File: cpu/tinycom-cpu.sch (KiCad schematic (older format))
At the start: 15 parts, among them P1 CONN_02X08, P2 CONN_02X08, U1 OLIMEX_IC_A13, U2 H5TQ2G83BFR/FBGA82, Y1 Crystal

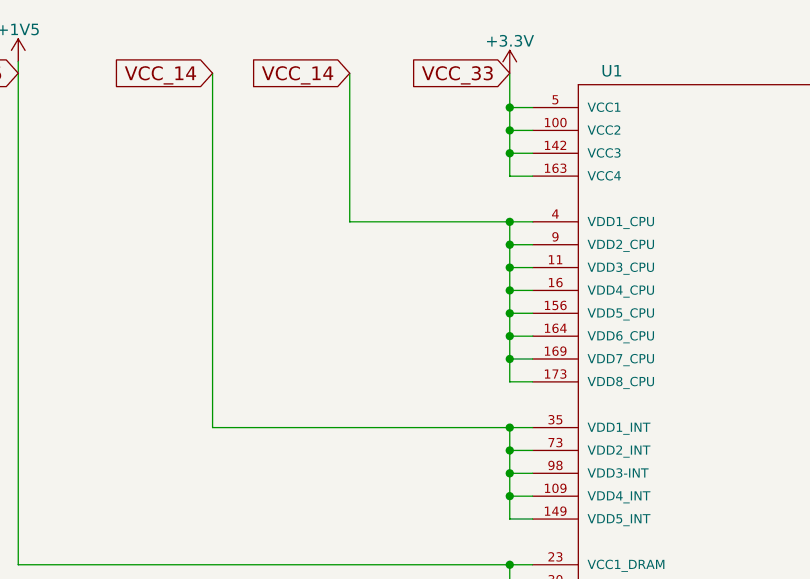
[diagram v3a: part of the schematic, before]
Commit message: add more capacitors
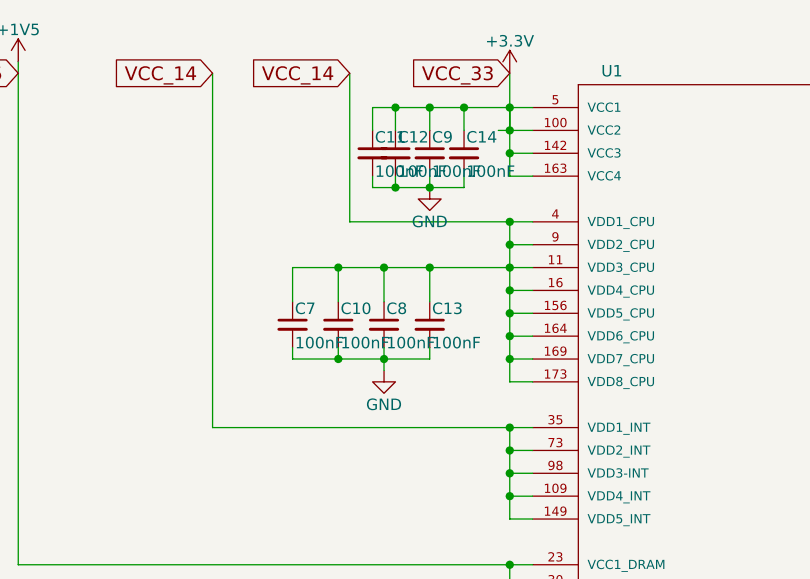
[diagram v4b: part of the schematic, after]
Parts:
- added C10, C11, C12, C13, C14, C7, C8, C9: 100nF, Capacitors_SMD:C_0603, symbol C_Small
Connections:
- net +3V3: now also C11.1, C12.1, C14.1, C9.1
- net GND: now also C10.2, C11.2, C12.2, C13.2, C14.2, C7.2, C8.2, C9.2
- net VCC_14: now also C10.1, C13.1, C7.1, C8.1
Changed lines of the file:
@@
 VCC_33
 $Comp
-L GND #PWR4
+L GND #PWR5
 U 1 1 5624C2D0
 P 1150 2350
-F 0 "#PWR4" H 1150 2100 50  0001 C CNN
+F 0 "#PWR5" H 1150 2100 50  0001 C CNN
 F 1 "GND" H 1150 2200 50  0000 C CNN
 F 2 "" H 1150 2350 60  0000 C CNN
@@
 VCC_14
 $Comp
-L +3.3V #PWR5
+L +3.3V #PWR7
 U 1 1 5624CB40
 P 1550 -1650
-F 0 "#PWR5" H 1550 -1800 50  0001 C CNN
+F 0 "#PWR7" H 1550 -1800 50  0001 C CNN
 F 1 "+3.3V" H 1550 -1510 50  0000 C CNN
 F 2 "" H 1550 -1650 60  0000 C CNN
@@
 DDR3_BA2
 $Comp
-L +1V5 #PWR14
+L +1V5 #PWR16
 U 1 1 5625F72C
 P 9350 -250
-F 0 "#PWR14" H 9350 -400 50  0001 C CNN
+F 0 "#PWR16" H 9350 -400 50  0001 C CNN
 F 1 "+1V5" H 9350 -110 50  0000 C CNN
 F 2 "" H 9350 -250 60  0000 C CNN
@@
 $EndComp
 $Comp
-L GND #PWR15
+L GND #PWR17
 U 1 1 5625F96A
 P 9500 3350
-F 0 "#PWR15" H 9500 3100 50  0001 C CNN
+F 0 "#PWR17" H 9500 3100 50  0001 C CNN
 F 1 "GND" H 9500 3200 50  0000 C CNN
 F 2 "" H 9500 3350 60  0000 C CNN
@@
 DDR3_RST
 $Comp
-L GND #PWR9
+L GND #PWR11
 U 1 1 5625FBB8
 P 5950 2100
-F 0 "#PWR9" H 5950 1850 50  0001 C CNN
+F 0 "#PWR11" H 5950 1850 50  0001 C CNN
 F 1 "GND" H 5950 1950 50  0000 C CNN
 F 2 "" H 5950 2100 60  0000 C CNN
@@
 $EndComp
 $Comp
-L +1V5 #PWR10
+L +1V5 #PWR12
 U 1 1 5625FE07
 P 6150 3250
-F 0 "#PWR10" H 6150 3100 50  0001 C CNN
+F 0 "#PWR12" H 6150 3100 50  0001 C CNN
 F 1 "+1V5" H 6150 3390 50  0000 C CNN
 F 2 "" H 6150 3250 60  0000 C CNN
@@
 $EndComp
 $Comp
-L GND #PWR11
+L GND #PWR13
 U 1 1 5625FF1B
 P 6150 4000
-F 0 "#PWR11" H 6150 3750 50  0001 C CNN
+F 0 "#PWR13" H 6150 3750 50  0001 C CNN
 F 1 "GND" H 6150 3850 50  0000 C CNN
 F 2 "" H 6150 4000 60  0000 C CNN
@@
 $EndComp
 $Comp
-L GND #PWR12
+L GND #PWR14
 U 1 1 56260662
 P 6400 4250
-F 0 "#PWR12" H 6400 4000 50  0001 C CNN
+F 0 "#PWR14" H 6400 4000 50  0001 C CNN
 F 1 "GND" H 6400 4100 50  0000 C CNN
 F 2 "" H 6400 4250 60  0000 C CNN
@@
 NoConn ~ 9250 3500
 $Comp
-L GND #PWR13
+L GND #PWR15
 U 1 1 56261679
 P 6600 4050
-F 0 "#PWR13" H 6600 3800 50  0001 C CNN
+F 0 "#PWR15" H 6600 3800 50  0001 C CNN
 F 1 "GND" H 6600 3900 50  0000 C CNN
 F 2 "" H 6600 4050 60  0000 C CNN
@@
 NoConn ~ 1650 4100
 $Comp
-L GND #PWR6
+L GND #PWR8
 U 1 1 56262629
 P 1550 2500
-F 0 "#PWR6" H 1550 2250 50  0001 C CNN
+F 0 "#PWR8" H 1550 2250 50  0001 C CNN
 F 1 "GND" H 1550 2350 50  0000 C CNN
 F 2 "" H 1550 2500 60  0000 C CNN
@@
 $EndComp
 $Comp
-L GND #PWR8
+L GND #PWR10
 U 1 1 56262930
 P 5550 3750
-F 0 "#PWR8" H 5550 3500 50  0001 C CNN
+F 0 "#PWR10" H 5550 3500 50  0001 C CNN
 F 1 "GND" H 5550 3600 50  0000 C CNN
 F 2 "" H 5550 3750 60  0000 C CNN
@@
 $EndComp
 $Comp
-L GND #PWR7
+L GND #PWR9
 U 1 1 56262D84
 P 5250 4100
-F 0 "#PWR7" H 5250 3850 50  0001 C CNN
+F 0 "#PWR9" H 5250 3850 50  0001 C CNN
 F 1 "GND" H 5250 3950 50  0000 C CNN
 F 2 "" H 5250 4100 60  0000 C CNN
@@
 $EndComp
 $Comp
-L +1V5 #PWR16
+L +1V5 #PWR18
 U 1 1 562642D9
 P 10200 -350
-F 0 "#PWR16" H 10200 -500 50  0001 C CNN
+F 0 "#PWR18" H 10200 -500 50  0001 C CNN
 F 1 "+1V5" H 10200 -210 50  0000 C CNN
 F 2 "" H 10200 -350 60  0000 C CNN
@@
 $EndComp
 $Comp
-L GND #PWR17
+L GND #PWR19
 U 1 1 562643A7
 P 10250 50
-F 0 "#PWR17" H 10250 -200 50  0001 C CNN
+F 0 "#PWR19" H 10250 -200 50  0001 C CNN
 F 1 "GND" H 10250 -100 50  0000 C CNN
 F 2 "" H 10250 50  60  0000 C CNN
@@
 $EndComp
 Wire Wire Line
-	1650 -1500 1550 -1500
+	950  -1500 1650 -1500
 Wire Wire Line
 	1550 -1650 1550 -1200
@@
 Connection ~ 1550 -1300
 Wire Wire Line
-	1650 -1400 1550 -1400
+	1500 -1400 1650 -1400
 Connection ~ 1550 -1400
 Wire Wire Line
@@
 Connection ~ 1550 -700
 Wire Wire Line
-	1650 -800 1550 -800
+	600  -800 1650 -800
 Connection ~ 1550 -800
 Wire Wire Line
@@
 	10250 50   10250 0
 Connection ~ 10250 0
+$Comp
+L C_Small C9
+U 1 1 56265419
+P 1200 -1300
+F 0 "C9" H 1210 -1230 50  0000 L CNN
+F 1 "100nF" H 1210 -1380 50  0000 L CNN
+F 2 "Capacitors_SMD:C_0603" H 1200 -1300 60  0001 C CNN
+F 3 "" H 1200 -1300 60  0000 C CNN
+	1    1200 -1300
+	1    0    0    -1
+$EndComp
+$Comp
+L C_Small C8
+U 1 1 562658F3
+P 1000 -550
+F 0 "C8" H 1010 -480 50  0000 L CNN
+F 1 "100nF" H 1010 -630 50  0000 L CNN
+F 2 "Capacitors_SMD:C_0603" H 1000 -550 60  0001 C CNN
+F 3 "" H 1000 -550 60  0000 C CNN
+	1    1000 -550
+	1    0    0    -1
+$EndComp
+$Comp
+L GND #PWR4
+U 1 1 56265943
+P 1000 -350
+F 0 "#PWR4" H 1000 -600 50  0001 C CNN
+F 1 "GND" H 1000 -500 50  0000 C CNN
+F 2 "" H 1000 -350 60  0000 C CNN
+F 3 "" H 1000 -350 60  0000 C CNN
+	1    1000 -350
+	1    0    0    -1
+$EndComp
+$Comp
+L GND #PWR6
+U 1 1 56265988
+P 1200 -1150
+F 0 "#PWR6" H 1200 -1400 50  0001 C CNN
+F 1 "GND" H 1200 -1300 50  0000 C CNN
+F 2 "" H 1200 -1150 60  0000 C CNN
+F 3 "" H 1200 -1150 60  0000 C CNN
+	1    1200 -1150
+	1    0    0    -1
+$EndComp
+Wire Wire Line
+	1200 -1200 1200 -1150
+Wire Wire Line
+	1000 -450 1000 -350
+Wire Wire Line
+	1550 -1500 1550 -1400
+Wire Wire Line
+	1200 -1400 1200 -1500
+Wire Wire Line
+	1000 -650 1000 -800
+$Comp
+L C_Small C14
+U 1 1 56266A58
+P 1350 -1300
+F 0 "C14" H 1360 -1230 50  0000 L CNN
+F 1 "100nF" H 1360 -1380 50  0000 L CNN
+F 2 "Capacitors_SMD:C_0603" H 1350 -1300 60  0001 C CNN
+F 3 "" H 1350 -1300 60  0000 C CNN
+	1    1350 -1300
+	1    0    0    -1
+$EndComp
+$Comp
+L C_Small C12
+U 1 1 56266AAE
+P 1050 -1300
+F 0 "C12" H 1060 -1230 50  0000 L CNN
+F 1 "100nF" H 1060 -1380 50  0000 L CNN
+F 2 "Capacitors_SMD:C_0603" H 1050 -1300 60  0001 C CNN
+F 3 "" H 1050 -1300 60  0000 C CNN
+	1    1050 -1300
+	1    0    0    -1
+$EndComp
+Wire Wire Line
+	1050 -1500 1050 -1400
+Connection ~ 1200 -1500
+Wire Wire Line
+	1350 -1400 1350 -1500
+Connection ~ 1350 -1500
+Wire Wire Line
+	1050 -1200 1050 -1150
+Wire Wire Line
+	950  -1150 1350 -1150
+Wire Wire Line
+	1350 -1150 1350 -1200
+Connection ~ 1200 -1150
+$Comp
+L C_Small C11
+U 1 1 56267024
+P 950 -1300
+F 0 "C11" H 960 -1230 50  0000 L CNN
+F 1 "100nF" H 960 -1380 50  0000 L CNN
+F 2 "Capacitors_SMD:C_0603" H 950 -1300 60  0001 C CNN
+F 3 "" H 950 -1300 60  0000 C CNN
+	1    950  -1300
+	1    0    0    -1
+$EndComp
+Wire Wire Line
+	950  -1500 950  -1400
+Connection ~ 1050 -1500
+Wire Wire Line
+	950  -1200 950  -1150
+Connection ~ 1050 -1150
+$Comp
+L C_Small C10
+U 1 1 56267401
+P 800 -550
+F 0 "C10" H 810 -480 50  0000 L CNN
+F 1 "100nF" H 810 -630 50  0000 L CNN
+F 2 "Capacitors_SMD:C_0603" H 800 -550 60  0001 C CNN
+F 3 "" H 800 -550 60  0000 C CNN
+	1    800  -550
+	1    0    0    -1
+$EndComp
+$Comp
+L C_Small C13
+U 1 1 56267464
+P 1200 -550
+F 0 "C13" H 1210 -480 50  0000 L CNN
+F 1 "100nF" H 1210 -630 50  0000 L CNN
+F 2 "Capacitors_SMD:C_0603" H 1200 -550 60  0001 C CNN
+F 3 "" H 1200 -550 60  0000 C CNN
+	1    1200 -550
+	1    0    0    -1
+$EndComp
+$Comp
+L C_Small C7
+U 1 1 562674C6
+P 600 -550
+F 0 "C7" H 610 -480 50  0000 L CNN
+F 1 "100nF" H 610 -630 50  0000 L CNN
+F 2 "Capacitors_SMD:C_0603" H 600 -550 60  0001 C CNN
+F 3 "" H 600 -550 60  0000 C CNN
+	1    600  -550
+	1    0    0    -1
+$EndComp
+Wire Wire Line
+	600  -800 600  -650
+Connection ~ 1000 -800
+Wire Wire Line
+	800  -650 800  -800
+Connection ~ 800  -800
+Wire Wire Line
+	1200 -650 1200 -800
+Connection ~ 1200 -800
+Wire Wire Line
+	600  -450 600  -400
+Wire Wire Line
+	600  -400 1200 -400
+Connection ~ 1000 -400
+Wire Wire Line
+	1200 -400 1200 -450
+Wire Wire Line
+	800  -400 800  -450
+Connection ~ 800  -400
 $EndSCHEMATC

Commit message: change to 0805 components
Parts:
- C1, C10, C11, C12, C13, C14, C2, C3, C4, C5, C6, C7, C8, C9: footprint Capacitors_SMD:C_0603 -> Capacitors_SMD:C_0805
- R1, R2, R3, R4: footprint Resistors_SMD:R_0603 -> Resistors_SMD:R_0805
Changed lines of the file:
@@
 VCC_33
 $Comp
-L GND #PWR5
+L GND #PWR01
 U 1 1 5624C2D0
 P 1150 2350
-F 0 "#PWR5" H 1150 2100 50  0001 C CNN
+F 0 "#PWR01" H 1150 2100 50  0001 C CNN
 F 1 "GND" H 1150 2200 50  0000 C CNN
 F 2 "" H 1150 2350 60  0000 C CNN
@@
 $EndComp
 $Comp
-L GND #PWR2
+L GND #PWR02
 U 1 1 5624C74D
 P 550 1900
-F 0 "#PWR2" H 550 1650 50  0001 C CNN
+F 0 "#PWR02" H 550 1650 50  0001 C CNN
 F 1 "GND" H 550 1750 50  0000 C CNN
 F 2 "" H 550 1900 60  0000 C CNN
@@
 $EndComp
 $Comp
-L GND #PWR3
+L GND #PWR03
 U 1 1 5624C778
 P 550 2200
-F 0 "#PWR3" H 550 1950 50  0001 C CNN
+F 0 "#PWR03" H 550 1950 50  0001 C CNN
 F 1 "GND" H 550 2050 50  0000 C CNN
 F 2 "" H 550 2200 60  0000 C CNN
@@
 F 0 "C1" H 810 1920 50  0000 L CNN
 F 1 "33pF" H 810 1770 50  0000 L CNN
-F 2 "Capacitors_SMD:C_0603" H 800 1850 60  0001 C CNN
+F 2 "Capacitors_SMD:C_0805" H 800 1850 60  0001 C CNN
 F 3 "" H 800 1850 60  0000 C CNN
 	1    800  1850
@@
 F 0 "C2" H 810 2220 50  0000 L CNN
 F 1 "33pF" H 810 2070 50  0000 L CNN
-F 2 "Capacitors_SMD:C_0603" H 800 2150 60  0001 C CNN
+F 2 "Capacitors_SMD:C_0805" H 800 2150 60  0001 C CNN
 F 3 "" H 800 2150 60  0000 C CNN
 	1    800  2150
@@
 VCC_14
 $Comp
-L +3.3V #PWR7
+L +3.3V #PWR04
 U 1 1 5624CB40
 P 1550 -1650
-F 0 "#PWR7" H 1550 -1800 50  0001 C CNN
+F 0 "#PWR04" H 1550 -1800 50  0001 C CNN
 F 1 "+3.3V" H 1550 -1510 50  0000 C CNN
 F 2 "" H 1550 -1650 60  0000 C CNN
@@
 $EndComp
 $Comp
-L +1V5 #PWR1
+L +1V5 #PWR05
 U 1 1 5624CB62
 P -600 -1700
-F 0 "#PWR1" H -600 -1850 50  0001 C CNN
+F 0 "#PWR05" H -600 -1850 50  0001 C CNN
 F 1 "+1V5" H -600 -1560 50  0000 C CNN
 F 2 "" H -600 -1700 60  0000 C CNN
@@
 DDR3_BA2
 $Comp
-L +1V5 #PWR16
+L +1V5 #PWR06
 U 1 1 5625F72C
 P 9350 -250
-F 0 "#PWR16" H 9350 -400 50  0001 C CNN
+F 0 "#PWR06" H 9350 -400 50  0001 C CNN
 F 1 "+1V5" H 9350 -110 50  0000 C CNN
 F 2 "" H 9350 -250 60  0000 C CNN
@@
 $EndComp
 $Comp
-L GND #PWR17
+L GND #PWR07
 U 1 1 5625F96A
 P 9500 3350
-F 0 "#PWR17" H 9500 3100 50  0001 C CNN
+F 0 "#PWR07" H 9500 3100 50  0001 C CNN
 F 1 "GND" H 9500 3200 50  0000 C CNN
 F 2 "" H 9500 3350 60  0000 C CNN
@@
 DDR3_RST
 $Comp
-L GND #PWR11
+L GND #PWR08
 U 1 1 5625FBB8
 P 5950 2100
-F 0 "#PWR11" H 5950 1850 50  0001 C CNN
+F 0 "#PWR08" H 5950 1850 50  0001 C CNN
 F 1 "GND" H 5950 1950 50  0000 C CNN
 F 2 "" H 5950 2100 60  0000 C CNN
@@
 $EndComp
 $Comp
-L +1V5 #PWR12
+L +1V5 #PWR09
 U 1 1 5625FE07
 P 6150 3250
-F 0 "#PWR12" H 6150 3100 50  0001 C CNN
+F 0 "#PWR09" H 6150 3100 50  0001 C CNN
 F 1 "+1V5" H 6150 3390 50  0000 C CNN
 F 2 "" H 6150 3250 60  0000 C CNN
@@
 F 0 "R1" V 6230 3450 50  0000 C CNN
 F 1 "1K" V 6150 3450 50  0000 C CNN
-F 2 "Resistors_SMD:R_0603" V 6080 3450 30  0001 C CNN
+F 2 "Resistors_SMD:R_0805" V 6080 3450 30  0001 C CNN
 F 3 "" H 6150 3450 30  0000 C CNN
 	1    6150 3450
@@
 F 0 "R2" V 6230 3800 50  0000 C CNN
 F 1 "1K" V 6150 3800 50  0000 C CNN
-F 2 "Resistors_SMD:R_0603" V 6080 3800 30  0001 C CNN
+F 2 "Resistors_SMD:R_0805" V 6080 3800 30  0001 C CNN
 F 3 "" H 6150 3800 30  0000 C CNN
 	1    6150 3800
@@
 $EndComp
 $Comp
-L GND #PWR13
+L GND #PWR010
 U 1 1 5625FF1B
 P 6150 4000
-F 0 "#PWR13" H 6150 3750 50  0001 C CNN
+F 0 "#PWR010" H 6150 3750 50  0001 C CNN
 F 1 "GND" H 6150 3850 50  0000 C CNN
 F 2 "" H 6150 4000 60  0000 C CNN
@@
 F 0 "R3" V 6480 4050 50  0000 C CNN
 F 1 "240R" V 6400 4050 50  0000 C CNN
-F 2 "Resistors_SMD:R_0603" V 6330 4050 30  0001 C CNN
+F 2 "Resistors_SMD:R_0805" V 6330 4050 30  0001 C CNN
 F 3 "" H 6400 4050 30  0000 C CNN
 	1    6400 4050
@@
 $EndComp
 $Comp
-L GND #PWR14
+L GND #PWR011
 U 1 1 56260662
 P 6400 4250
-F 0 "#PWR14" H 6400 4000 50  0001 C CNN
+F 0 "#PWR011" H 6400 4000 50  0001 C CNN
 F 1 "GND" H 6400 4100 50  0000 C CNN
 F 2 "" H 6400 4250 60  0000 C CNN
@@
 NoConn ~ 9250 3500
 $Comp
-L GND #PWR15
+L GND #PWR012
 U 1 1 56261679
 P 6600 4050
-F 0 "#PWR15" H 6600 3800 50  0001 C CNN
+F 0 "#PWR012" H 6600 3800 50  0001 C CNN
 F 1 "GND" H 6600 3900 50  0000 C CNN
 F 2 "" H 6600 4050 60  0000 C CNN
@@
 NoConn ~ 1650 4100
 $Comp
-L GND #PWR8
+L GND #PWR013
 U 1 1 56262629
 P 1550 2500
-F 0 "#PWR8" H 1550 2250 50  0001 C CNN
+F 0 "#PWR013" H 1550 2250 50  0001 C CNN
 F 1 "GND" H 1550 2350 50  0000 C CNN
 F 2 "" H 1550 2500 60  0000 C CNN
@@
 $EndComp
 $Comp
-L GND #PWR10
+L GND #PWR014
 U 1 1 56262930
 P 5550 3750
-F 0 "#PWR10" H 5550 3500 50  0001 C CNN
+F 0 "#PWR014" H 5550 3500 50  0001 C CNN
 F 1 "GND" H 5550 3600 50  0000 C CNN
 F 2 "" H 5550 3750 60  0000 C CNN
@@
 F 0 "R4" V 5330 3900 50  0000 C CNN
 F 1 "240R" V 5250 3900 50  0000 C CNN
-F 2 "Resistors_SMD:R_0603" V 5180 3900 30  0001 C CNN
+F 2 "Resistors_SMD:R_0805" V 5180 3900 30  0001 C CNN
 F 3 "" H 5250 3900 30  0000 C CNN
 	1    5250 3900
@@
 $EndComp
 $Comp
-L GND #PWR9
+L GND #PWR015
 U 1 1 56262D84
 P 5250 4100
-F 0 "#PWR9" H 5250 3850 50  0001 C CNN
+F 0 "#PWR015" H 5250 3850 50  0001 C CNN
 F 1 "GND" H 5250 3950 50  0000 C CNN
 F 2 "" H 5250 4100 60  0000 C CNN
@@
 F 0 "C3" H 9910 -80 50  0000 L CNN
 F 1 "100nF" H 9910 -230 50  0000 L CNN
-F 2 "Capacitors_SMD:C_0603" H 9900 -150 60  0001 C CNN
+F 2 "Capacitors_SMD:C_0805" H 9900 -150 60  0001 C CNN
 F 3 "" H 9900 -150 60  0000 C CNN
 	1    9900 -150
@@
 F 0 "C4" H 10110 -80 50  0000 L CNN
 F 1 "100nF" H 10110 -230 50  0000 L CNN
-F 2 "Capacitors_SMD:C_0603" H 10100 -150 60  0001 C CNN
+F 2 "Capacitors_SMD:C_0805" H 10100 -150 60  0001 C CNN
 F 3 "" H 10100 -150 60  0000 C CNN
 	1    10100 -150
@@
 F 0 "C5" H 10310 -80 50  0000 L CNN
 F 1 "100nF" H 10310 -230 50  0000 L CNN
-F 2 "Capacitors_SMD:C_0603" H 10300 -150 60  0001 C CNN
+F 2 "Capacitors_SMD:C_0805" H 10300 -150 60  0001 C CNN
 F 3 "" H 10300 -150 60  0000 C CNN
 	1    10300 -150
@@
 F 0 "C6" H 10510 -80 50  0000 L CNN
 F 1 "100nF" H 10510 -230 50  0000 L CNN
-F 2 "Capacitors_SMD:C_0603" H 10500 -150 60  0001 C CNN
+F 2 "Capacitors_SMD:C_0805" H 10500 -150 60  0001 C CNN
 F 3 "" H 10500 -150 60  0000 C CNN
 	1    10500 -150
@@
 $EndComp
 $Comp
-L +1V5 #PWR18
+L +1V5 #PWR016
 U 1 1 562642D9
 P 10200 -350
-F 0 "#PWR18" H 10200 -500 50  0001 C CNN
+F 0 "#PWR016" H 10200 -500 50  0001 C CNN
 F 1 "+1V5" H 10200 -210 50  0000 C CNN
 F 2 "" H 10200 -350 60  0000 C CNN
@@
 $EndComp
 $Comp
-L GND #PWR19
+L GND #PWR017
 U 1 1 562643A7
 P 10250 50
-F 0 "#PWR19" H 10250 -200 50  0001 C CNN
+F 0 "#PWR017" H 10250 -200 50  0001 C CNN
 F 1 "GND" H 10250 -100 50  0000 C CNN
 F 2 "" H 10250 50  60  0000 C CNN
@@
 F 0 "C9" H 1210 -1230 50  0000 L CNN
 F 1 "100nF" H 1210 -1380 50  0000 L CNN
-F 2 "Capacitors_SMD:C_0603" H 1200 -1300 60  0001 C CNN
+F 2 "Capacitors_SMD:C_0805" H 1200 -1300 60  0001 C CNN
 F 3 "" H 1200 -1300 60  0000 C CNN
 	1    1200 -1300
@@
 F 0 "C8" H 1010 -480 50  0000 L CNN
 F 1 "100nF" H 1010 -630 50  0000 L CNN
-F 2 "Capacitors_SMD:C_0603" H 1000 -550 60  0001 C CNN
+F 2 "Capacitors_SMD:C_0805" H 1000 -550 60  0001 C CNN
 F 3 "" H 1000 -550 60  0000 C CNN
 	1    1000 -550
@@
 $EndComp
 $Comp
-L GND #PWR4
+L GND #PWR018
 U 1 1 56265943
 P 1000 -350
-F 0 "#PWR4" H 1000 -600 50  0001 C CNN
+F 0 "#PWR018" H 1000 -600 50  0001 C CNN
 F 1 "GND" H 1000 -500 50  0000 C CNN
 F 2 "" H 1000 -350 60  0000 C CNN
@@
 $EndComp
 $Comp
-L GND #PWR6
+L GND #PWR019
 U 1 1 56265988
 P 1200 -1150
-F 0 "#PWR6" H 1200 -1400 50  0001 C CNN
+F 0 "#PWR019" H 1200 -1400 50  0001 C CNN
 F 1 "GND" H 1200 -1300 50  0000 C CNN
 F 2 "" H 1200 -1150 60  0000 C CNN
@@
 F 0 "C14" H 1360 -1230 50  0000 L CNN
 F 1 "100nF" H 1360 -1380 50  0000 L CNN
-F 2 "Capacitors_SMD:C_0603" H 1350 -1300 60  0001 C CNN
+F 2 "Capacitors_SMD:C_0805" H 1350 -1300 60  0001 C CNN
 F 3 "" H 1350 -1300 60  0000 C CNN
 	1    1350 -1300
@@
 F 0 "C12" H 1060 -1230 50  0000 L CNN
 F 1 "100nF" H 1060 -1380 50  0000 L CNN
-F 2 "Capacitors_SMD:C_0603" H 1050 -1300 60  0001 C CNN
+F 2 "Capacitors_SMD:C_0805" H 1050 -1300 60  0001 C CNN
 F 3 "" H 1050 -1300 60  0000 C CNN
 	1    1050 -1300
@@
 F 0 "C11" H 960 -1230 50  0000 L CNN
 F 1 "100nF" H 960 -1380 50  0000 L CNN
-F 2 "Capacitors_SMD:C_0603" H 950 -1300 60  0001 C CNN
+F 2 "Capacitors_SMD:C_0805" H 950 -1300 60  0001 C CNN
 F 3 "" H 950 -1300 60  0000 C CNN
 	1    950  -1300
@@
 F 0 "C10" H 810 -480 50  0000 L CNN
 F 1 "100nF" H 810 -630 50  0000 L CNN
-F 2 "Capacitors_SMD:C_0603" H 800 -550 60  0001 C CNN
+F 2 "Capacitors_SMD:C_0805" H 800 -550 60  0001 C CNN
 F 3 "" H 800 -550 60  0000 C CNN
 	1    800  -550
@@
 F 0 "C13" H 1210 -480 50  0000 L CNN
 F 1 "100nF" H 1210 -630 50  0000 L CNN
-F 2 "Capacitors_SMD:C_0603" H 1200 -550 60  0001 C CNN
+F 2 "Capacitors_SMD:C_0805" H 1200 -550 60  0001 C CNN
 F 3 "" H 1200 -550 60  0000 C CNN
 	1    1200 -550
@@
 F 0 "C7" H 610 -480 50  0000 L CNN
 F 1 "100nF" H 610 -630 50  0000 L CNN
-F 2 "Capacitors_SMD:C_0603" H 600 -550 60  0001 C CNN
+F 2 "Capacitors_SMD:C_0805" H 600 -550 60  0001 C CNN
 F 3 "" H 600 -550 60  0000 C CNN
 	1    600  -550

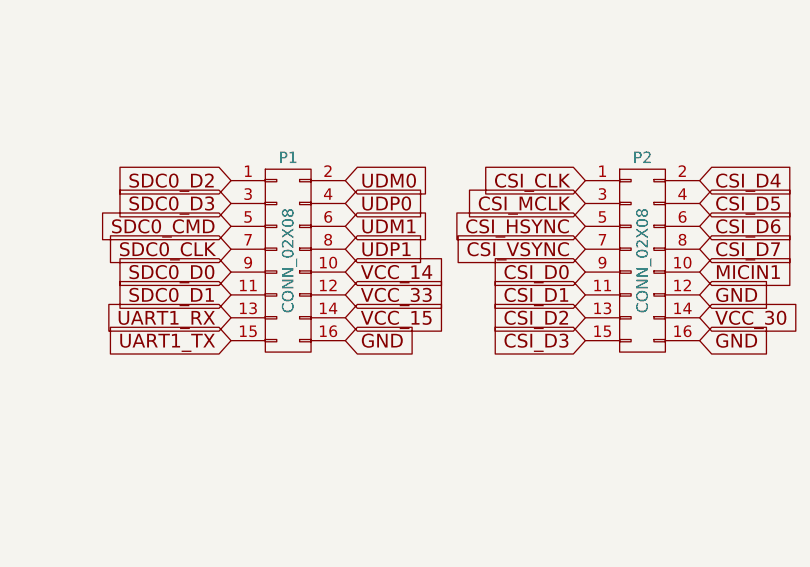
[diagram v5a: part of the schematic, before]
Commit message: add power planes
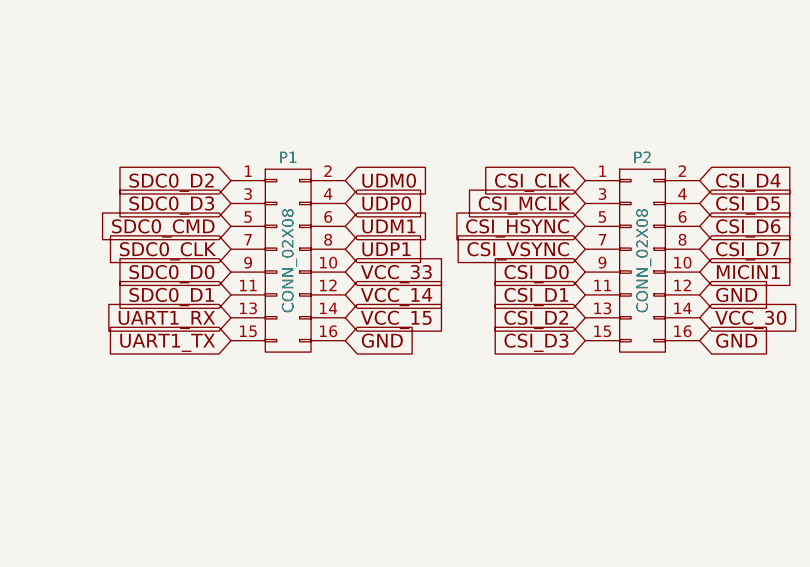
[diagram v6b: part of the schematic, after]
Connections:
- net +3V3: now also P1.10 (P10); no longer P1.12 (P12)
- net VCC_14: now also P1.12 (P12); no longer P1.10 (P10)
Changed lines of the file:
@@
 VCC_15
 Text GLabel 7850 5900 2    60   Input ~ 0
+VCC_14
+Text GLabel 7850 5800 2    60   Input ~ 0
 VCC_33
-Text GLabel 7850 5800 2    60   Input ~ 0
-VCC_14
 Text GLabel 9400 6000 2    60   Input ~ 0
 VCC_30

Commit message: svref fix
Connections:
- net +3V3: now also U1.157 (UBOOT), U1.158 (NMI_N), U1.159 (RESET_N)
- net GND: no longer U1.157 (UBOOT), U1.159 (RESET_N), U1.18 (SVREF)
- net SVREF: now reaches R1.2, R2.1, U2.E1 (VREFDQ), U2.J8 (VREFCA)
- net SVREF: now also U1.18 (SVREF)
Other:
- moved on the sheet: C1, C10, C11, C12, C13, C14, C2, C3, C4, C5, C6, C7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
